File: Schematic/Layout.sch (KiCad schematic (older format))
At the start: 27 parts, among them J1 JTAG, J2 Power, U1 RF430FRL

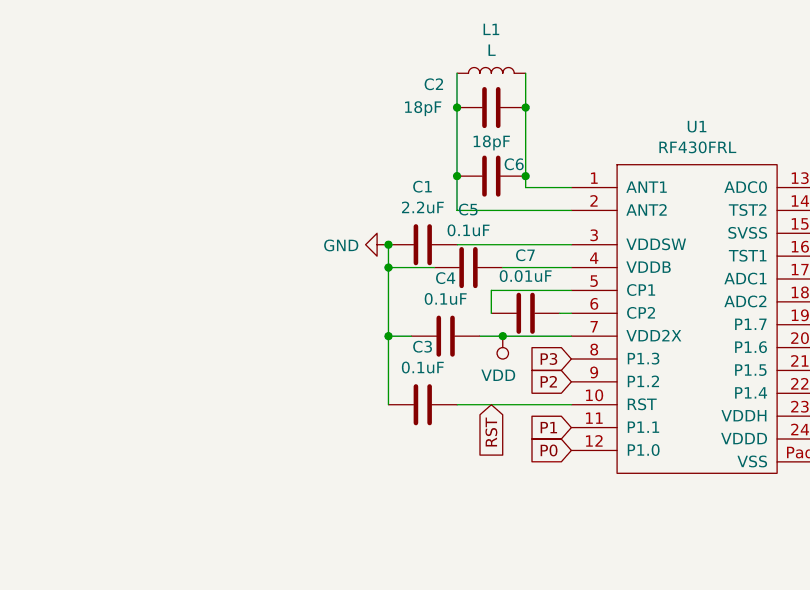
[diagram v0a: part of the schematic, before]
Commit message: Finished and ordered V1
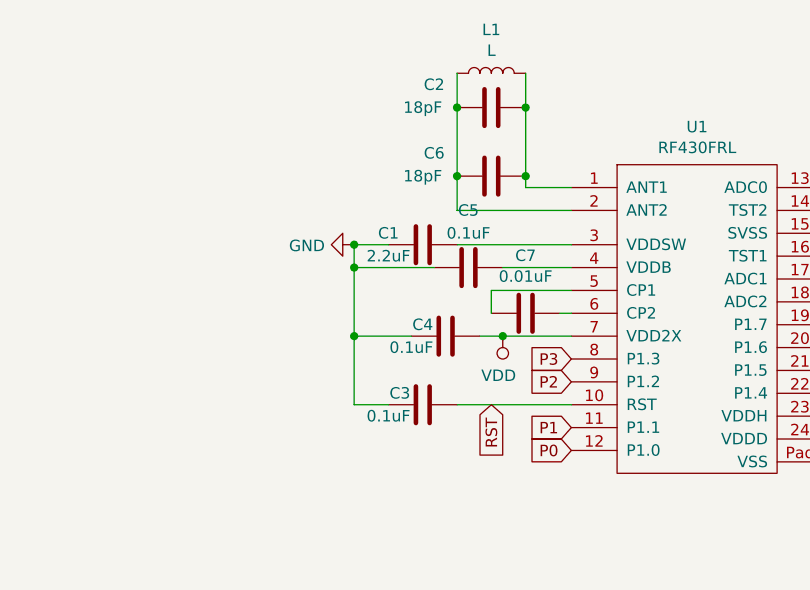
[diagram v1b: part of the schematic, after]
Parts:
- J1: footprint (none) -> NFCBusiness:Jtag
- J2: footprint (none) -> NFCBusiness:PwrPins
- L1: footprint (none) -> NFCBusiness:Layout
- U1: footprint (none) -> Housings_DFN_QFN:QFN-24_4x4mm_Pitch0.5mm_NoMask
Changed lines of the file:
@@
 LIBS:power
 LIBS:74xx
+LIBS:Layout-cache
 EELAYER 26 0
 EELAYER END
@@
 F 0 "U1" H 8350 3265 50  0000 C CNN
 F 1 "RF430FRL" H 8350 3174 50  0000 C CNN
-F 2 "" H 8350 2650 50  0001 C CNN
+F 2 "Housings_DFN_QFN:QFN-24_4x4mm_Pitch0.5mm_NoMask" H 8350 2650 50  0001 C CNN
 F 3 "" H 8350 2650 50  0001 C CNN
 	1    8350 2650
@@
 F 0 "L1" V 7640 1800 50  0000 C CNN
 F 1 "L" V 7549 1800 50  0000 C CNN
-F 2 "" H 7450 1800 50  0001 C CNN
+F 2 "NFCBusiness:Layout" H 7450 1800 50  0001 C CNN
 F 3 "~" H 7450 1800 50  0001 C CNN
 	1    7450 1800
@@
 	7300 1800 7300 1950
 Wire Wire Line
-	7300 2400 7800 2400
-Wire Wire Line
 	7800 2300 7600 2300
 Wire Wire Line
@@
 U 1 1 5C18DACD
 P 7150 2550
-F 0 "C1" V 6898 2550 50  0000 C CNN
-F 1 "2.2uF" V 6989 2550 50  0000 C CNN
+F 0 "C1" V 7100 2400 50  0000 C CNN
+F 1 "2.2uF" V 7200 2400 50  0000 C CNN
 F 2 "Capacitors_SMD:C_0805" H 7188 2400 50  0001 C CNN
 F 3 "~" H 7150 2550 50  0001 C CNN
@@
 L power:GND #PWR01
 U 1 1 5C18DB75
-P 7000 2550
-F 0 "#PWR01" H 7000 2300 50  0001 C CNN
-F 1 "GND" V 7005 2422 50  0000 R CNN
-F 2 "" H 7000 2550 50  0001 C CNN
-F 3 "" H 7000 2550 50  0001 C CNN
-	1    7000 2550
+P 6850 2550
+F 0 "#PWR01" H 6850 2300 50  0001 C CNN
+F 1 "GND" V 6855 2422 50  0000 R CNN
+F 2 "" H 6850 2550 50  0001 C CNN
+F 3 "" H 6850 2550 50  0001 C CNN
+	1    6850 2550
 	0    1    1    0
 $EndComp
@@
 U 1 1 5C18DBC1
 P 7350 2650
-F 0 "C5" V 7098 2650 50  0000 C CNN
-F 1 "0.1uF" V 7189 2650 50  0000 C CNN
+F 0 "C5" V 7100 2650 50  0000 C CNN
+F 1 "0.1uF" V 7200 2650 50  0000 C CNN
 F 2 "Capacitors_SMD:C_0805" H 7388 2500 50  0001 C CNN
 F 3 "~" H 7350 2650 50  0001 C CNN
@@
 	0    1    1    0
 $EndComp
-Wire Wire Line
-	7200 2650 7000 2650
-Wire Wire Line
-	7000 2650 7000 2550
-Connection ~ 7000 2550
 Wire Wire Line
 	7500 2650 7800 2650
@@
 U 1 1 5C18DE93
 P 7250 2950
-F 0 "C4" V 6998 2950 50  0000 C CNN
-F 1 "0.1uF" V 7089 2950 50  0000 C CNN
+F 0 "C4" V 7200 2850 50  0000 C CNN
+F 1 "0.1uF" V 7300 2800 50  0000 C CNN
 F 2 "Capacitors_SMD:C_0805" H 7288 2800 50  0001 C CNN
 F 3 "~" H 7250 2950 50  0001 C CNN
@@
 	0    1    1    0
 $EndComp
-Wire Wire Line
-	7100 2950 7000 2950
-Wire Wire Line
-	7000 2950 7000 2650
-Connection ~ 7000 2650
 $Comp
 L Device:C C3
 U 1 1 5C18E108
 P 7150 3250
-F 0 "C3" V 6898 3250 50  0000 C CNN
-F 1 "0.1uF" V 6989 3250 50  0000 C CNN
+F 0 "C3" V 7100 3150 50  0000 C CNN
+F 1 "0.1uF" V 7200 3100 50  0000 C CNN
 F 2 "Capacitors_SMD:C_0805" H 7188 3100 50  0001 C CNN
 F 3 "~" H 7150 3250 50  0001 C CNN
@@
 	0    1    1    0
 $EndComp
-Wire Wire Line
-	7000 3250 7000 2950
-Connection ~ 7000 2950
 Wire Wire Line
 	7300 3250 7800 3250
@@
 U 1 1 5C18ED62
 P 7450 2250
-F 0 "C6" V 7400 2350 50  0000 C CNN
-F 1 "18pF" V 7300 2250 50  0000 C CNN
+F 0 "C6" V 7350 2000 50  0000 C CNN
+F 1 "18pF" V 7450 1950 50  0000 C CNN
 F 2 "Capacitors_SMD:C_0805" H 7488 2100 50  0001 C CNN
 F 3 "~" H 7450 2250 50  0001 C CNN
@@
 F 0 "J1" H 2200 2417 50  0000 C CNN
 F 1 "JTAG" H 2200 2326 50  0000 C CNN
-F 2 "" H 2150 2100 50  0001 C CNN
+F 2 "NFCBusiness:Jtag" H 2150 2100 50  0001 C CNN
 F 3 "~" H 2150 2100 50  0001 C CNN
 	1    2150 2100
@@
 F 0 "J2" H 2020 2725 50  0000 C CNN
 F 1 "Power" H 2020 2816 50  0000 C CNN
-F 2 "" H 2100 3050 50  0001 C CNN
+F 2 "NFCBusiness:PwrPins" H 2100 3050 50  0001 C CNN
 F 3 "~" H 2100 3050 50  0001 C CNN
 	1    2100 3050
@@
 	1    0    0    -1
 $EndComp
+Wire Wire Line
+	7000 3250 6850 3250
+Wire Wire Line
+	6850 3250 6850 2950
+Wire Wire Line
+	6850 2550 7000 2550
+Connection ~ 6850 2550
+Wire Wire Line
+	6850 2650 7200 2650
+Connection ~ 6850 2650
+Wire Wire Line
+	6850 2650 6850 2550
+Wire Wire Line
+	6850 2950 7100 2950
+Connection ~ 6850 2950
+Wire Wire Line
+	6850 2950 6850 2650
+Wire Wire Line
+	7300 2400 7800 2400
 $EndSCHEMATC

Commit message: Changed programming footprint to use VDDSW
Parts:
- U1: symbol MCU_Texas_MSP430:RF430FRL -> Layout-rescue:RF430FRL-MCU_Texas_MSP430
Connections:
- net VDD: no longer J2.2 (Pin_2)
- net VDDA: now reaches C1.1, U1.3 (VDDSW)
- net VDDA: now also J2.2 (Pin_2)
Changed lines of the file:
@@
 $EndDescr
 $Comp
-L MCU_Texas_MSP430:RF430FRL U1
+L Layout-rescue:RF430FRL-MCU_Texas_MSP430 U1
 U 1 1 5C18D6DB
 P 8350 2650
@@
 $EndComp
 Wire Wire Line
-	7300 2550 7800 2550
+	7300 2550 7700 2550
 $Comp
 L power:GND #PWR01
@@
 $EndComp
 $Comp
-L power:VDD #PWR09
-U 1 1 5C2BDF49
-P 2300 2950
-F 0 "#PWR09" H 2300 2800 50  0001 C CNN
-F 1 "VDD" V 2317 3078 50  0000 L CNN
-F 2 "" H 2300 2950 50  0001 C CNN
-F 3 "" H 2300 2950 50  0001 C CNN
-	1    2300 2950
-	0    1    1    0
-$EndComp
-$Comp
 L power:GND #PWR010
 U 1 1 5C2BE03D
@@
 Wire Wire Line
 	7300 2400 7800 2400
+$Comp
+L power:VDDA #PWR0101
+U 1 1 5C34F964
+P 7700 2550
+F 0 "#PWR0101" H 7700 2400 50  0001 C CNN
+F 1 "VDDA" H 7700 2700 50  0000 C CNN
+F 2 "" H 7700 2550 50  0001 C CNN
+F 3 "" H 7700 2550 50  0001 C CNN
+	1    7700 2550
+	1    0    0    -1
+$EndComp
+Connection ~ 7700 2550
+Wire Wire Line
+	7700 2550 7800 2550
+$Comp
+L power:VDDA #PWR0102
+U 1 1 5C34FBCF
+P 2300 2950
+F 0 "#PWR0102" H 2300 2800 50  0001 C CNN
+F 1 "VDDA" V 2317 3078 50  0000 L CNN
+F 2 "" H 2300 2950 50  0001 C CNN
+F 3 "" H 2300 2950 50  0001 C CNN
+	1    2300 2950
+	0    1    1    0
+$EndComp
 $EndSCHEMATC

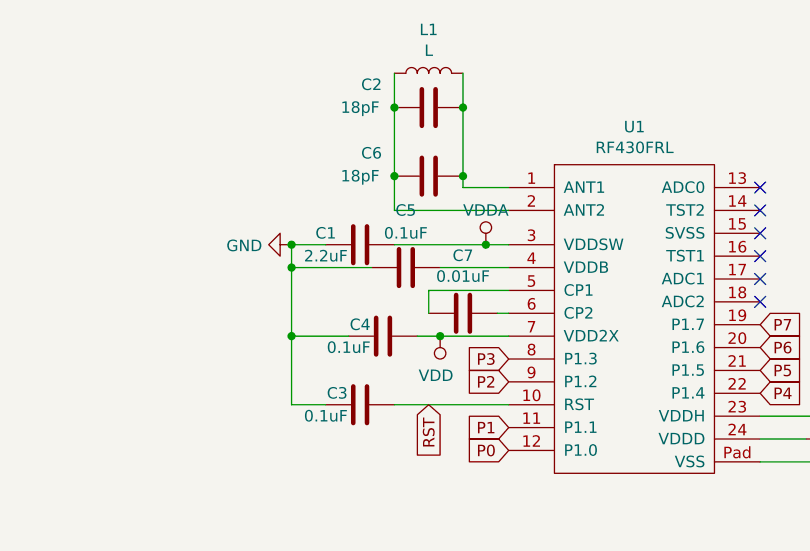
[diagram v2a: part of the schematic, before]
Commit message: Changed pcb antenna to match proper inductance
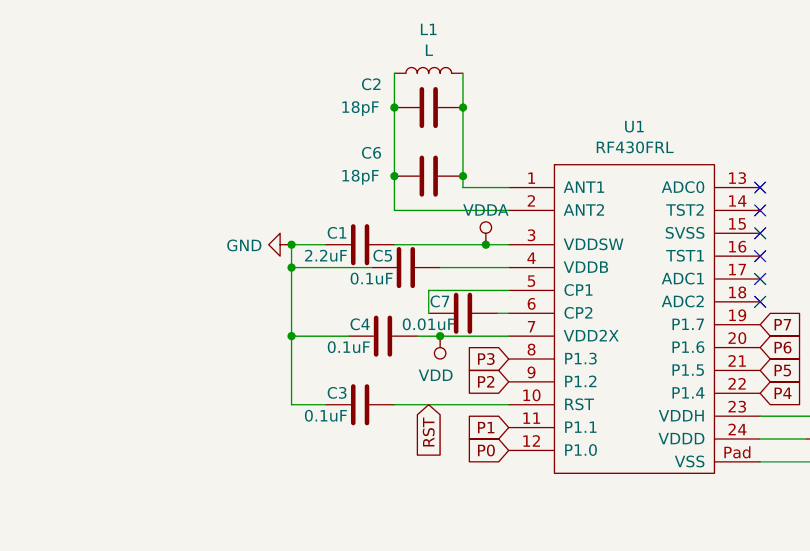
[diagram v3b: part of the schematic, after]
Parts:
- U1: footprint Housings_DFN_QFN:QFN-24_4x4mm_Pitch0.5mm_NoMask -> Housings_DFN_QFN:QFN-24-1EP_4x4mm_Pitch0.5mm
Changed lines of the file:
@@
 F 0 "U1" H 8350 3265 50  0000 C CNN
 F 1 "RF430FRL" H 8350 3174 50  0000 C CNN
-F 2 "Housings_DFN_QFN:QFN-24_4x4mm_Pitch0.5mm_NoMask" H 8350 2650 50  0001 C CNN
+F 2 "Housings_DFN_QFN:QFN-24-1EP_4x4mm_Pitch0.5mm" H 8350 2650 50  0001 C CNN
 F 3 "" H 8350 2650 50  0001 C CNN
 	1    8350 2650
@@
 U 1 1 5C18DACD
 P 7150 2550
-F 0 "C1" V 7100 2400 50  0000 C CNN
+F 0 "C1" V 7100 2450 50  0000 C CNN
 F 1 "2.2uF" V 7200 2400 50  0000 C CNN
 F 2 "Capacitors_SMD:C_0805" H 7188 2400 50  0001 C CNN
@@
 U 1 1 5C18DBC1
 P 7350 2650
-F 0 "C5" V 7100 2650 50  0000 C CNN
-F 1 "0.1uF" V 7200 2650 50  0000 C CNN
+F 0 "C5" V 7300 2550 50  0000 C CNN
+F 1 "0.1uF" V 7400 2500 50  0000 C CNN
 F 2 "Capacitors_SMD:C_0805" H 7388 2500 50  0001 C CNN
 F 3 "~" H 7350 2650 50  0001 C CNN
@@
 U 1 1 5C18DD20
 P 7600 2850
-F 0 "C7" V 7348 2850 50  0000 C CNN
-F 1 "0.01uF" V 7439 2850 50  0000 C CNN
+F 0 "C7" V 7550 2750 50  0000 C CNN
+F 1 "0.01uF" V 7650 2700 50  0000 C CNN
 F 2 "Capacitors_SMD:C_0805" H 7638 2700 50  0001 C CNN
 F 3 "~" H 7600 2850 50  0001 C CNN
